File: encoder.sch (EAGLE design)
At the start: 5 parts, among them IC1 MEGA8-AI, SW1 EC12E_SW, U1 MAX485CSA+

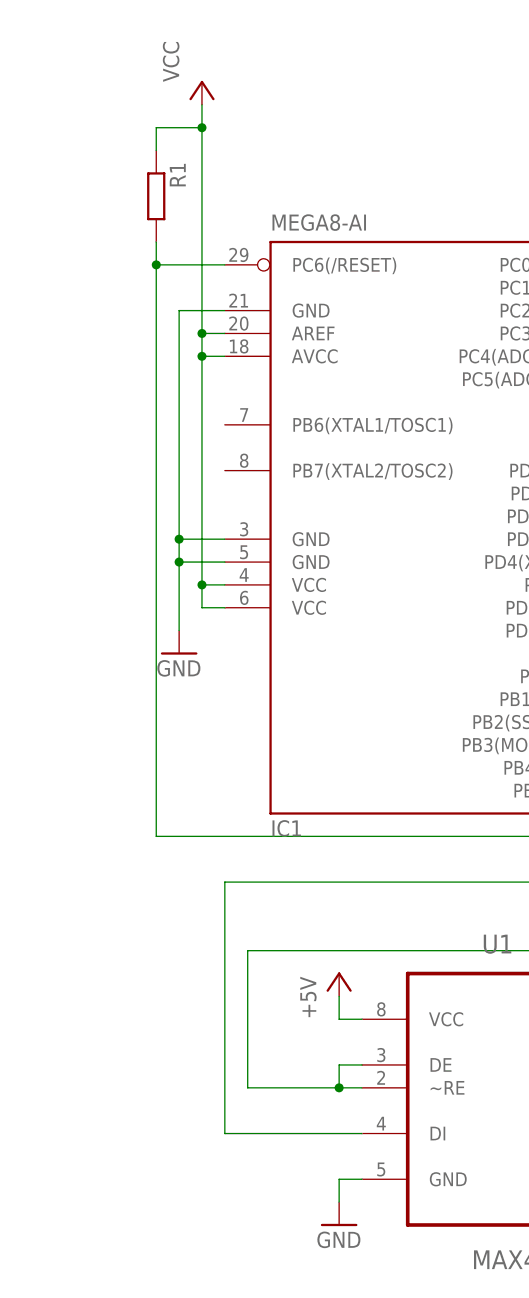
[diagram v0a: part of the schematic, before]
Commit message: Допиливание железа
Подтяжки TX на Vcc, забытый резистор на верхнем транзисторе в драйвере,
конденсаторы на питание МК, подписи элементов в разводке
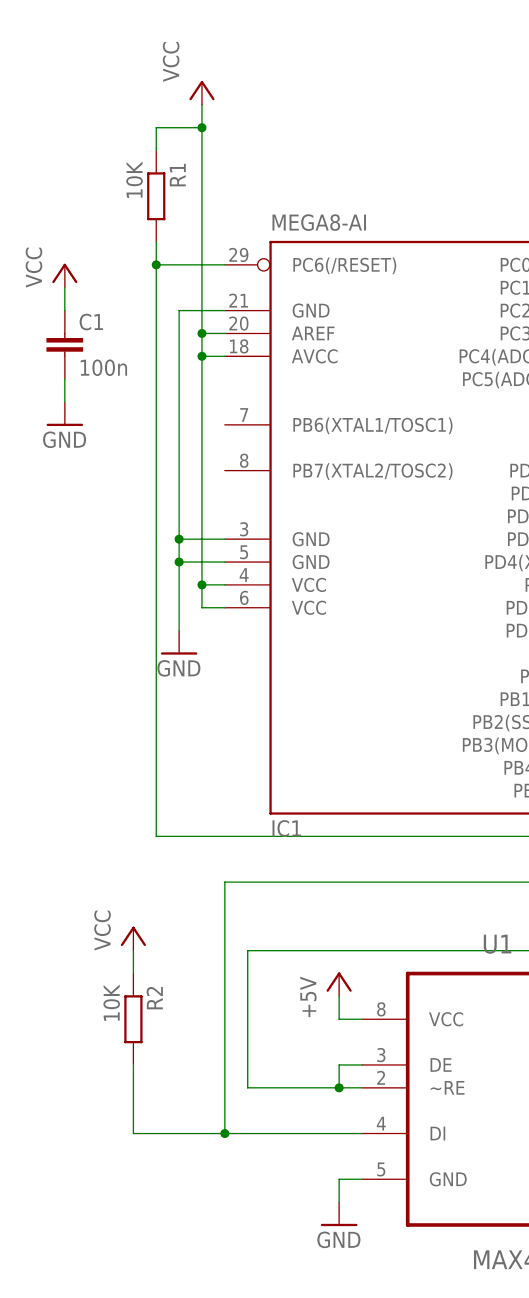
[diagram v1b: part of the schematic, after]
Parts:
- added C1: 100n, capacitor-wima:C2,5-3
- added R2: 10K, resistor:R-EU_M1206
- R1: value (none) -> 10K
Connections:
- net GND: now also C1.2
- net N$1: now also R2.2
- net VCC: now also C1.1, R2.1
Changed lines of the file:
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@@
 <part name="GND2" library="supply1" deviceset="GND" device=""/>
 <part name="P+4" library="supply1" deviceset="VCC" device=""/>
-<part name="R1" library="resistor" deviceset="R-EU_" device="M1206"/>
+<part name="R1" library="resistor" deviceset="R-EU_" device="M1206" value="10K"/>
 <part name="GND3" library="supply1" deviceset="GND" device=""/>
+<part name="R2" library="resistor" deviceset="R-EU_" device="M1206" value="10K"/>
+<part name="P+5" library="supply1" deviceset="VCC" device=""/>
+<part name="P+6" library="supply1" deviceset="VCC" device=""/>
+<part name="GND4" library="supply1" deviceset="GND" device=""/>
+<part name="C1" library="capacitor-wima" deviceset="C" device="2,5-3" value="100n"/>
 </parts>
 <sheets>
@@
 <instance part="R1" gate="G$1" x="10.16" y="106.68" rot="R270"/>
 <instance part="GND3" gate="1" x="12.7" y="55.88"/>
+<instance part="R2" gate="G$1" x="7.62" y="15.24" rot="R270"/>
+<instance part="P+5" gate="VCC" x="7.62" y="25.4" smashed="yes">
+<attribute name="VALUE" x="5.08" y="22.86" size="1.778" layer="96" rot="R90"/>
+</instance>
+<instance part="P+6" gate="VCC" x="0" y="99.06" smashed="yes">
+<attribute name="VALUE" x="-2.54" y="96.52" size="1.778" layer="96" rot="R90"/>
+</instance>
+<instance part="GND4" gate="1" x="0" y="81.28"/>
+<instance part="C1" gate="G$1" x="0" y="91.44"/>
 </instances>
 <busses>
@@
 <pinref part="IC1" gate="G$1" pin="PD1(TXD)"/>
 <wire x1="66.04" y1="73.66" x2="88.9" y2="73.66" width="0.1524" layer="91"/>
+<pinref part="R2" gate="G$1" pin="2"/>
+<wire x1="17.78" y1="2.54" x2="7.62" y2="2.54" width="0.1524" layer="91"/>
+<wire x1="7.62" y1="2.54" x2="7.62" y2="10.16" width="0.1524" layer="91"/>
+<junction x="17.78" y="2.54"/>
 </segment>
 </net>
@@
 <junction x="15.24" y="114.3"/>
 </segment>
+<segment>
+<pinref part="R2" gate="G$1" pin="1"/>
+<pinref part="P+5" gate="VCC" pin="VCC"/>
+<wire x1="7.62" y1="20.32" x2="7.62" y2="22.86" width="0.1524" layer="91"/>
+</segment>
+<segment>
+<pinref part="C1" gate="G$1" pin="1"/>
+<pinref part="P+6" gate="VCC" pin="VCC"/>
+<wire x1="0" y1="93.98" x2="0" y2="96.52" width="0.1524" layer="91"/>
+</segment>
 </net>
 <net name="GND" class="0">
@@
 <junction x="12.7" y="68.58"/>
 </segment>
+<segment>
+<pinref part="GND4" gate="1" pin="GND"/>
+<pinref part="C1" gate="G$1" pin="2"/>
+<wire x1="0" y1="83.82" x2="0" y2="86.36" width="0.1524" layer="91"/>
+</segment>
 </net>

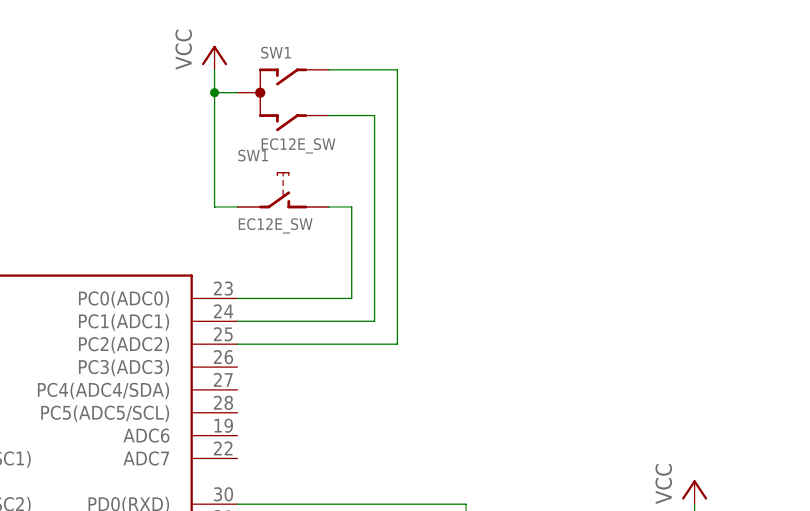
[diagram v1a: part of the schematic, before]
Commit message: изменение разводки под энкодер
энкодер на землю, подтягивающие резисторы к плюсу
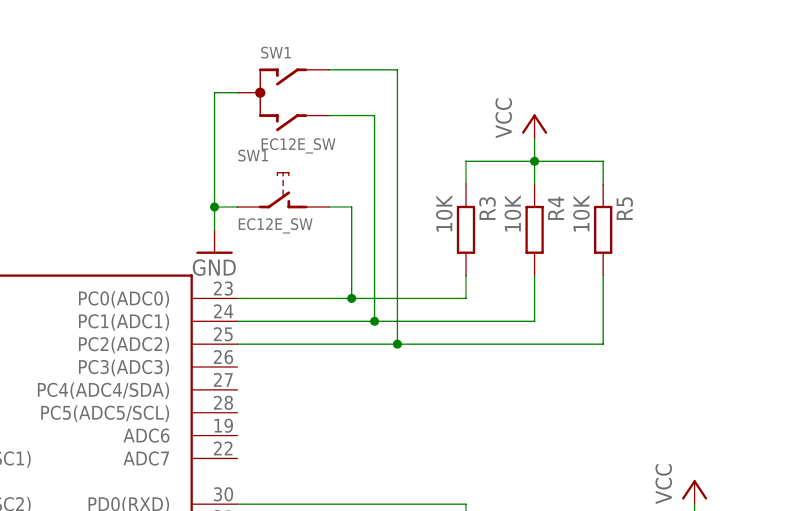
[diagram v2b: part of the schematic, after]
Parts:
- added R3, R4, R5: 10K, resistor:R-EU_M1206
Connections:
- net GND: now also SW1G$1.C, SW1G$2.2
- net N$10: now also R3.2
- net N$5: now also R5.2
- net N$9: now also R4.2
- net VCC: now also R3.1, R4.1, R5.1; no longer SW1G$1.C, SW1G$2.2
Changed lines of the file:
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@@
 <part name="GND1" library="supply1" deviceset="GND" device=""/>
 <part name="SW1" library="switch-alps" deviceset="EC12E_SW" device=""/>
-<part name="P+3" library="supply1" deviceset="VCC" device=""/>
 <part name="U1" library="Maxim_By_element14_Batch_1" deviceset="MAX485CSA+" device=""/>
 <part name="P+1" library="supply1" deviceset="+5V" device=""/>
@@
 <part name="GND4" library="supply1" deviceset="GND" device=""/>
 <part name="C1" library="capacitor-wima" deviceset="C" device="2,5-3" value="100n"/>
+<part name="GND5" library="supply1" deviceset="GND" device=""/>
+<part name="R3" library="resistor" deviceset="R-EU_" device="M1206" value="10K"/>
+<part name="R4" library="resistor" deviceset="R-EU_" device="M1206" value="10K"/>
+<part name="R5" library="resistor" deviceset="R-EU_" device="M1206" value="10K"/>
+<part name="P+3" library="supply1" deviceset="VCC" device=""/>
 </parts>
 <sheets>
@@
 <instance part="SW1" gate="G$1" x="68.58" y="121.92" rot="R270"/>
 <instance part="SW1" gate="G$2" x="71.12" y="109.22"/>
-<instance part="P+3" gate="VCC" x="63.5" y="127" smashed="yes">
-<attribute name="VALUE" x="60.96" y="124.46" size="1.778" layer="96" rot="R90"/>
-</instance>
 <instance part="U1" gate="A" x="50.8" y="10.16"/>
 <instance part="P+1" gate="1" x="30.48" y="20.32"/>
@@
 <instance part="GND4" gate="1" x="0" y="81.28"/>
 <instance part="C1" gate="G$1" x="0" y="91.44"/>
+<instance part="GND5" gate="1" x="63.5" y="104.14"/>
+<instance part="R3" gate="G$1" x="91.44" y="106.68" rot="R270"/>
+<instance part="R4" gate="G$1" x="99.06" y="106.68" rot="R270"/>
+<instance part="R5" gate="G$1" x="106.68" y="106.68" rot="R270"/>
+<instance part="P+3" gate="VCC" x="99.06" y="119.38" smashed="yes">
+<attribute name="VALUE" x="96.52" y="116.84" size="1.778" layer="96" rot="R90"/>
+</instance>
 </instances>
 <busses>
@@
 </net>
 <net name="VCC" class="0">
-<segment>
-<pinref part="SW1" gate="G$2" pin="2"/>
-<wire x1="66.04" y1="109.22" x2="63.5" y2="109.22" width="0.1524" layer="91"/>
-<wire x1="63.5" y1="109.22" x2="63.5" y2="121.92" width="0.1524" layer="91"/>
-<pinref part="SW1" gate="G$1" pin="C"/>
-<wire x1="63.5" y1="121.92" x2="66.04" y2="121.92" width="0.1524" layer="91"/>
-<pinref part="P+3" gate="VCC" pin="VCC"/>
-<wire x1="63.5" y1="121.92" x2="63.5" y2="124.46" width="0.1524" layer="91"/>
-<junction x="63.5" y="121.92"/>
-</segment>
 <segment>
 <pinref part="ISP" gate="-2" pin="S"/>
@@
 <wire x1="0" y1="93.98" x2="0" y2="96.52" width="0.1524" layer="91"/>
 </segment>
+<segment>
+<pinref part="R3" gate="G$1" pin="1"/>
+<wire x1="91.44" y1="111.76" x2="91.44" y2="114.3" width="0.1524" layer="91"/>
+<wire x1="91.44" y1="114.3" x2="99.06" y2="114.3" width="0.1524" layer="91"/>
+<pinref part="R4" gate="G$1" pin="1"/>
+<wire x1="99.06" y1="114.3" x2="99.06" y2="111.76" width="0.1524" layer="91"/>
+<wire x1="99.06" y1="114.3" x2="106.68" y2="114.3" width="0.1524" layer="91"/>
+<pinref part="R5" gate="G$1" pin="1"/>
+<wire x1="106.68" y1="114.3" x2="106.68" y2="111.76" width="0.1524" layer="91"/>
+<pinref part="P+3" gate="VCC" pin="VCC"/>
+<wire x1="99.06" y1="114.3" x2="99.06" y2="116.84" width="0.1524" layer="91"/>
+<junction x="99.06" y="114.3"/>
+</segment>
 </net>
 <net name="GND" class="0">
@@
 <wire x1="0" y1="83.82" x2="0" y2="86.36" width="0.1524" layer="91"/>
 </segment>
+<segment>
+<pinref part="SW1" gate="G$2" pin="2"/>
+<wire x1="66.04" y1="109.22" x2="63.5" y2="109.22" width="0.1524" layer="91"/>
+<wire x1="63.5" y1="109.22" x2="63.5" y2="121.92" width="0.1524" layer="91"/>
+<pinref part="SW1" gate="G$1" pin="C"/>
+<wire x1="63.5" y1="121.92" x2="66.04" y2="121.92" width="0.1524" layer="91"/>
+<pinref part="GND5" gate="1" pin="GND"/>
+<wire x1="63.5" y1="106.68" x2="63.5" y2="109.22" width="0.1524" layer="91"/>
+<junction x="63.5" y="109.22"/>
+</segment>
 </net>
 <net name="N$5" class="0">
@@
 <pinref part="IC1" gate="G$1" pin="PC2(ADC2)"/>
 <wire x1="83.82" y1="93.98" x2="66.04" y2="93.98" width="0.1524" layer="91"/>
+<pinref part="R5" gate="G$1" pin="2"/>
+<wire x1="83.82" y1="93.98" x2="106.68" y2="93.98" width="0.1524" layer="91"/>
+<wire x1="106.68" y1="93.98" x2="106.68" y2="101.6" width="0.1524" layer="91"/>
+<junction x="83.82" y="93.98"/>
 </segment>
 </net>
@@
 <pinref part="IC1" gate="G$1" pin="PC1(ADC1)"/>
 <wire x1="66.04" y1="96.52" x2="81.28" y2="96.52" width="0.1524" layer="91"/>
+<pinref part="R4" gate="G$1" pin="2"/>
+<wire x1="81.28" y1="96.52" x2="99.06" y2="96.52" width="0.1524" layer="91"/>
+<wire x1="99.06" y1="96.52" x2="99.06" y2="101.6" width="0.1524" layer="91"/>
+<junction x="81.28" y="96.52"/>
 </segment>
 </net>
@@
 <pinref part="IC1" gate="G$1" pin="PC0(ADC0)"/>
 <wire x1="78.74" y1="99.06" x2="66.04" y2="99.06" width="0.1524" layer="91"/>
-</segment>
-</net>
+<pinref part="R3" gate="G$1" pin="2"/>
+<wire x1="78.74" y1="99.06" x2="91.44" y2="99.06" width="0.1524" layer="91"/>
+<wire x1="91.44" y1="99.06" x2="91.44" y2="101.6" width="0.1524" layer="91"/>
+<junction x="78.74" y="99.06"/>
+</segment>
+</net>
